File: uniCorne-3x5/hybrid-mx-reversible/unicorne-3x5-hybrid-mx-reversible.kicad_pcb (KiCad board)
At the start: 2 copper layers, 114.7 x 91.4 mm, 87 parts, among them J1 MJ-4PP-9, J2 Nice!View, J3 Conn_01x02, J4 Conn_01x03, SW1 SW_MX_HS, SW10 SW_MX_HS, SW11 SW_MX_HS, SW12 SW_MX_HS, SW13 SW_MX_HS, SW14 SW_MX_HS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

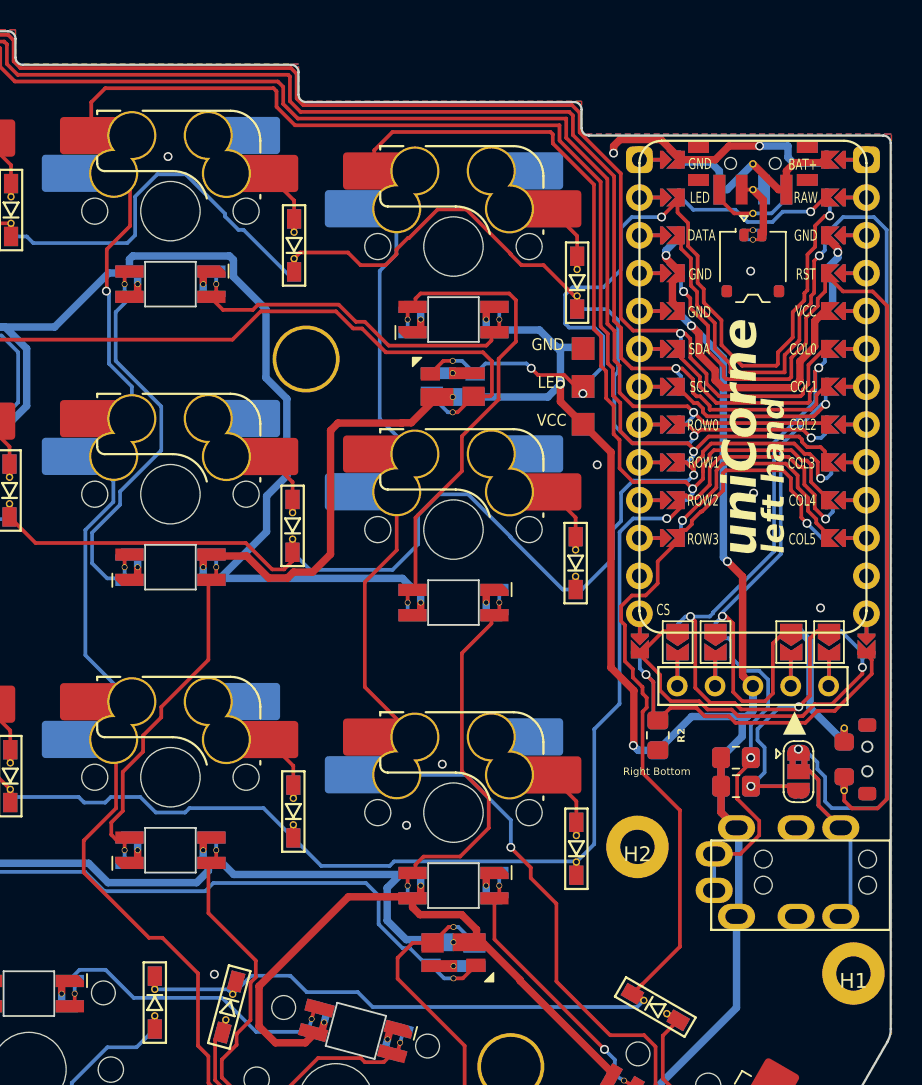
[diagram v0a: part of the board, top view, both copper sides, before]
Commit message: Bug fix scl (#3)
* fixed 3x5 hyprid mx

* fixed 3x5

* fixed 3x6
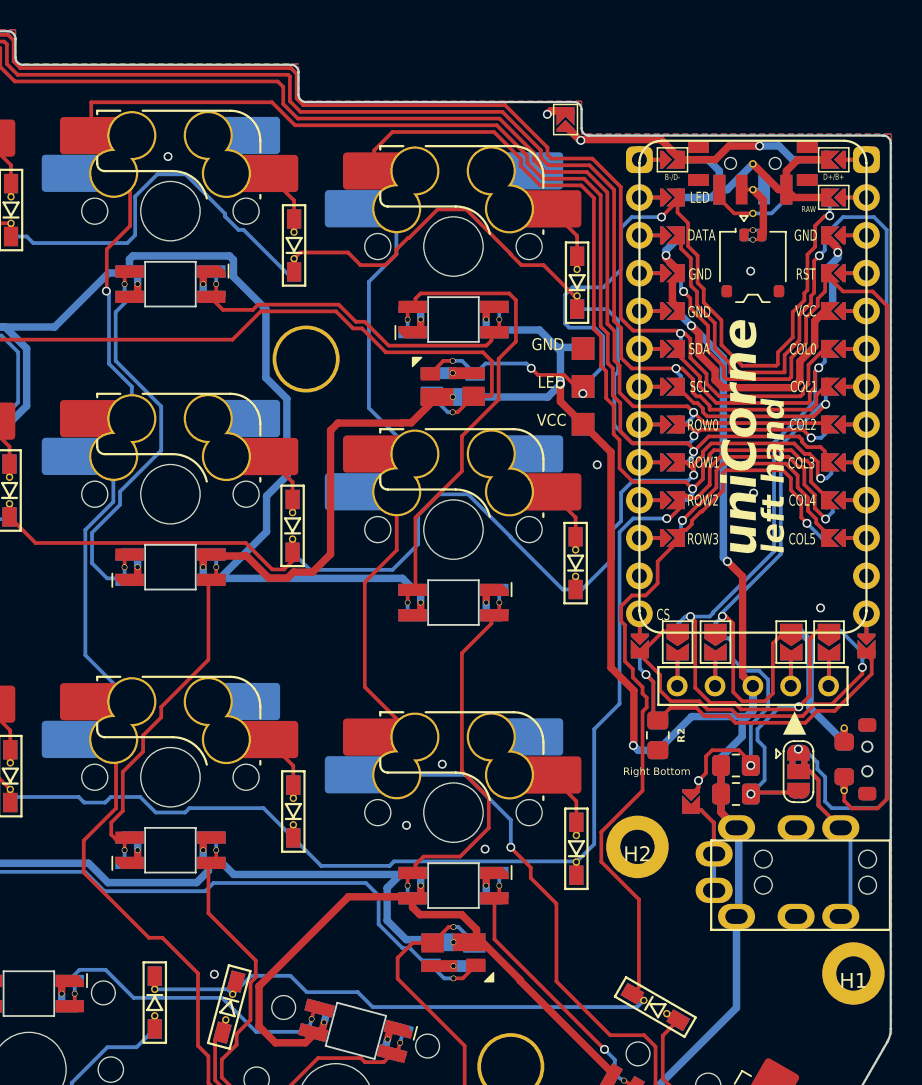
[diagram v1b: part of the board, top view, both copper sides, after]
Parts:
- added JP10: , TB2086_MISC:SolderJumper-2_P1.3mm_Open_TrianglePad1.0x1.2mm_rev, F.Cu at (181.3, 112.8)
- added JP11: , TB2086_MISC:SolderJumper-2_P1.3mm_Open_TrianglePad1.0x1.2mm_rev, F.Cu at (172.9, 67.0)
- U1: footprint TB2086_MISC:ProMicro-ish-dn-rev-unrouted_3x6 -> TB2086_MISC:ProMicro-ish-dn-rev-unrouted_3x5
- moved R3 0.53 mm to (184.3, 110.4)
- moved R4 0.52 mm to (184.3, 112.3)
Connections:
- J1 pad A: SCL -> Net-(JP10-B)
- U1 pad 24: unconnected-(U1-RAW-Pad24) -> BAT+
- U1 pad 26: GND -> B-/D-
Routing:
- net B-/D-: track 0.00 -> 20.6 mm, vias 0 -> 2
- net GND: track 38.3 -> 24.2 mm
- net unconnected-(U1-RAW-Pad24): track 11.0 -> 0.00 mm, vias 1 -> 0
- net Net-(JP10-B): track 0.00 -> 10.4 mm
- net BAT+: track 14.2 -> 19.8 mm
- net SCL: track 66.1 -> 62.5 mm, vias 3 -> 4
- net col3: track 152.1 -> 149.9 mm
- net col1: track 153.1 -> 152.1 mm
- net col0: track 174.0 -> 173.0 mm
- net col2: track 185.5 -> 184.5 mm
- net SDA: track 69.8 -> 70.8 mm
- net VCC: track 501.4 -> 500.8 mm
